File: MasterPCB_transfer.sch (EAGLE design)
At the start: 989 parts, among them IC1 NCS21911SN2T1G, IC10 LDL1117S33R, IC11 LTC4222CUH#PBF, IC12 LTC4222CUH#PBF, IC13 LTC4222CUH#PBF, IC14 LTC4222CUH#PBF, IC15 LTC4222CUH#PBF, IC16 LTC4222CUH#PBF, IC17 LTC4222CUH#PBF, IC18 LTC4222CUH#PBF, IC19 LTC4222CUH#PBF, IC2 NCS21911SN2T1G, IC20 LTC4222CUH#PBF, IC21 LTC4222CUH#PBF, IC22 LTC4222CUH#PBF, IC23 LTC4222CUH#PBF, IC24 NCS21911SN2T1G, IC25 NCS21911SN2T1G, IC26 NCS21911SN2T1G, IC27 NCS21911SN2T1G, IC28 NCS21911SN2T1G, IC29 NCS21911SN2T1G, IC3 NCS21911SN2T1G, IC30 NCS21911SN2T1G, IC31 ADIS16500AMLZ, IC32 LTC6820IUD#PBF, IC33 CBTL01023GM,115, IC34 S35ML04G300WHI000, IC35 S35ML04G300WHI000, IC36 S35ML04G300WHI000, IC37 S35ML04G300WHI000, IC38 ADS8588HIPM, IC39 S35ML04G300WHI000, IC4 LTC4222CUH#PBF, IC40 S35ML04G300WHI000, IC41 S35ML04G300WHI000, IC42 S35ML04G300WHI000, IC43 S35ML04G300WHI000, IC44 S35ML04G300WHI000, IC45 S35ML04G300WHI000, IC46 S35ML04G300WHI000, IC47 S35ML04G300WHI000, IC48 S35ML04G300WHI000, IC49 S35ML04G300WHI000, IC5 LP38692SDX-5.0_NOPB, IC50 S35ML04G300WHI000, IC51 ADS8588HIPM, IC52 ADS8588HIPM, IC55 MUX36S16IRSNR, IC6 LP38692SDX-5.0_NOPB, IC7 LDL1117S33R, IC8 LDL1117S33R, IC9 LP38692SDX-5.0_NOPB, J1 SAMTEC-SMM-104-02-X-DJ, J2 SAMTEC-CLP-106-02-X-DJ, J4 TFM-120-02-L-D, J5 TFM-120-02-L-D, J6 TFM-120-02-L-D, J7 TFM-120-02-L-D, J8 TFM-120-02-L-D, J9 SSM-109-L-SV, M1 NTLUS4C12NTAG, M10 NTLUS4C12NTAG, M11 NTLUS4C12NTAG, M12 NTLUS4C12NTAG, M13 NTLUS4C12NTAG, M14 NTLUS4C12NTAG, M15 NTLUS4C12NTAG, M16 NTLUS4C12NTAG, M17 NTLUS4C12NTAG, M18 NTLUS4C12NTAG, M19 NTLUS4C12NTAG, M2 NTLUS4C12NTAG, M20 NTLUS4C12NTAG, M21 NTLUS4C12NTAG, M22 NTLUS4C12NTAG, M23 NTLUS4C12NTAG, M24 NTLUS4C12NTAG, M25 NTLUS4C12NTAG, M26 NTLUS4C12NTAG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

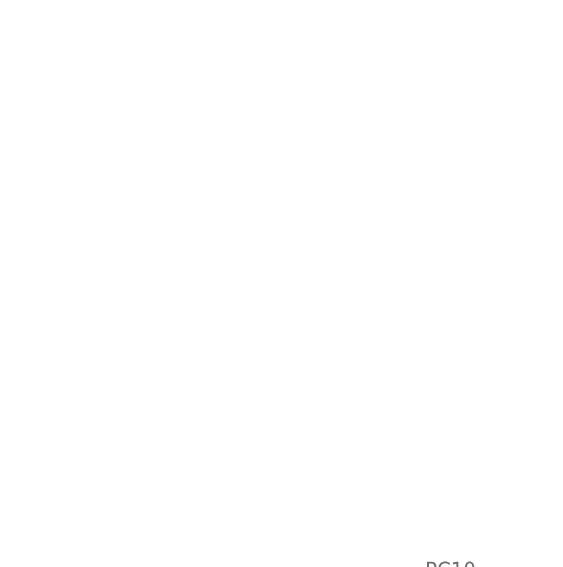
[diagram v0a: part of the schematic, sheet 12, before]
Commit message: Created solid works stripped model of board and setup main board to support layout
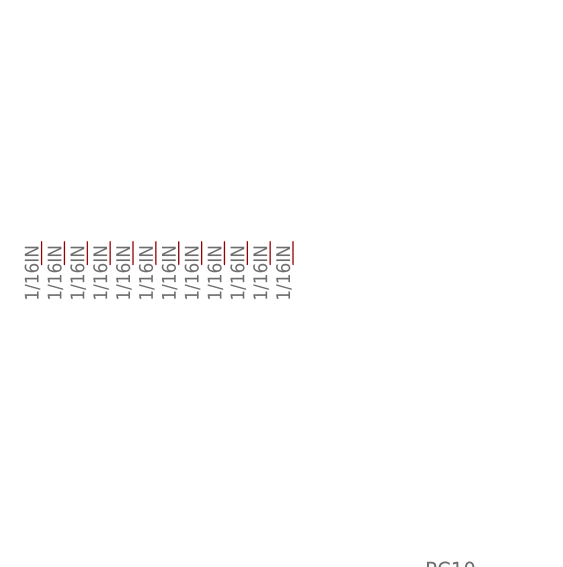
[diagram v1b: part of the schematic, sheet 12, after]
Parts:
- added U$10, U$11, U$12, U$13, U$14, U$15, U$16, U$5, U$6, U$7, U$8, U$9: THROUGH_HOLE, SamacSys_Parts:THROUGH_HOLE
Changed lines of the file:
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@@
 <part name="D87" library="SamacSys_Parts" library_urn="urn:adsk.eagle:library:31941355" deviceset="RSR025N03HZGTL" device="" package3d_urn="urn:adsk.eagle:package:34959477/2"/>
 <part name="J9" library="SamacSys_Parts" library_urn="urn:adsk.eagle:library:31941355" deviceset="SSM-109-L-SV" device="" package3d_urn="urn:adsk.eagle:package:34729422/5"/>
+<part name="U$5" library="SamacSys_Parts" library_urn="urn:adsk.eagle:library:31941355" deviceset="THROUGH_HOLE" device="" package3d_urn="urn:adsk.eagle:package:35094096/3"/>
+<part name="U$6" library="SamacSys_Parts" library_urn="urn:adsk.eagle:library:31941355" deviceset="THROUGH_HOLE" device="" package3d_urn="urn:adsk.eagle:package:35094096/3"/>
+<part name="U$7" library="SamacSys_Parts" library_urn="urn:adsk.eagle:library:31941355" deviceset="THROUGH_HOLE" device="" package3d_urn="urn:adsk.eagle:package:35094096/3"/>
+<part name="U$8" library="SamacSys_Parts" library_urn="urn:adsk.eagle:library:31941355" deviceset="THROUGH_HOLE" device="" package3d_urn="urn:adsk.eagle:package:35094096/3"/>
+<part name="U$9" library="SamacSys_Parts" library_urn="urn:adsk.eagle:library:31941355" deviceset="THROUGH_HOLE" device="" package3d_urn="urn:adsk.eagle:package:35094096/3"/>
+<part name="U$10" library="SamacSys_Parts" library_urn="urn:adsk.eagle:library:31941355" deviceset="THROUGH_HOLE" device="" package3d_urn="urn:adsk.eagle:package:35094096/3"/>
+<part name="U$11" library="SamacSys_Parts" library_urn="urn:adsk.eagle:library:31941355" deviceset="THROUGH_HOLE" device="" package3d_urn="urn:adsk.eagle:package:35094096/3"/>
+<part name="U$12" library="SamacSys_Parts" library_urn="urn:adsk.eagle:library:31941355" deviceset="THROUGH_HOLE" device="" package3d_urn="urn:adsk.eagle:package:35094096/3"/>
+<part name="U$13" library="SamacSys_Parts" library_urn="urn:adsk.eagle:library:31941355" deviceset="THROUGH_HOLE" device="" package3d_urn="urn:adsk.eagle:package:35094096/3"/>
+<part name="U$14" library="SamacSys_Parts" library_urn="urn:adsk.eagle:library:31941355" deviceset="THROUGH_HOLE" device="" package3d_urn="urn:adsk.eagle:package:35094096/3"/>
+<part name="U$15" library="SamacSys_Parts" library_urn="urn:adsk.eagle:library:31941355" deviceset="THROUGH_HOLE" device="" package3d_urn="urn:adsk.eagle:package:35094096/3"/>
+<part name="U$16" library="SamacSys_Parts" library_urn="urn:adsk.eagle:library:31941355" deviceset="THROUGH_HOLE" device="" package3d_urn="urn:adsk.eagle:package:35094096/3"/>
 </parts>
 <sheets>
@@
 <attribute name="VALUE" x="243.84" y="-12.7" size="1.778" layer="96"/>
 </instance>
+<instance part="U$5" gate="G$1" x="-30.48" y="132.08" smashed="yes"/>
+<instance part="U$6" gate="G$1" x="-33.02" y="132.08" smashed="yes"/>
+<instance part="U$7" gate="G$1" x="-35.56" y="132.08" smashed="yes"/>
+<instance part="U$8" gate="G$1" x="-38.1" y="132.08" smashed="yes"/>
+<instance part="U$9" gate="G$1" x="-40.64" y="132.08" smashed="yes"/>
+<instance part="U$10" gate="G$1" x="-43.18" y="132.08" smashed="yes"/>
+<instance part="U$11" gate="G$1" x="-45.72" y="132.08" smashed="yes"/>
+<instance part="U$12" gate="G$1" x="-48.26" y="132.08" smashed="yes"/>
+<instance part="U$13" gate="G$1" x="-50.8" y="132.08" smashed="yes"/>
+<instance part="U$14" gate="G$1" x="-53.34" y="132.08" smashed="yes"/>
+<instance part="U$15" gate="G$1" x="-25.4" y="132.08" smashed="yes"/>
+<instance part="U$16" gate="G$1" x="-27.94" y="132.08" smashed="yes"/>
 </instances>
 <busses>

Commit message: Moving pc, finsihed layout of 7 e-fuses
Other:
- note removed: "2x 16 bit differential single frame capture SAR ADCs that are dedicated for measuring simultaneous outputs from strain gauges. Input signal flow Analog signal -> High input impedance buffer -> Low pass filter BW@~200 hz -> High input impedance buffer -> Digitizing The ADC also applies a 3rd order low pass filter with built in oversampling functionalty. Communication occurs thorugh a serial line."
- note removed: "2x 16 bit differential single frame capture SAR ADCs that are dedicated for measuring simultaneous outputs from strain gauges. Input signal flow Analog signal -> High input impedance buffer -> Low pass filter BW@~200 hz -> High input impedance buffer -> scale input within 5v range -> Digitizing The ADC also applies a 3rd order low pass filter with built in oversampling functionalty. Communication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"
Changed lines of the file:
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@@
 <description>Strain Gauge ADC</description>
 <plain>
-<text x="66.04" y="508" size="1.778" layer="97">2x 16 bit differential single frame capture SAR ADCs that are dedicated for measuring simultaneous outputs from strain gauges.
-Input signal flow
-Analog signal -&gt; High input impedance buffer -&gt; Low pass filter BW@~200 hz -&gt; High input impedance buffer -&gt; Digitizing
-The ADC also applies a 3rd order low pass filter with built in oversampling functionalty.
-Communication occurs thorugh a serial line.</text>
-<rectangle x1="63.5" y1="495.3" x2="213.36" y2="530.86" layer="98"/>
 <text x="210.82" y="228.6" size="1.778" layer="97">From data sheet for split plane conditioning</text>
 <wire x1="208.28" y1="233.68" x2="208.28" y2="226.06" width="0.1524" layer="94"/>
@@
 <description>General and accelerometer ADC</description>
 <plain>
-<text x="30.48" y="233.68" size="1.778" layer="97">2x 16 bit differential single frame capture SAR ADCs that are dedicated for measuring simultaneous outputs from strain gauges.
-Input signal flow
-Analog signal -&gt; High input impedance buffer -&gt; Low pass filter BW@~200 hz -&gt; High input impedance buffer -&gt; scale input within 5v range -&gt; Digitizing
-The ADC also applies a 3rd order low pass filter with built in oversampling functionalty.
-Communication occurs thorugh a serial line.</text>
-<rectangle x1="25.4" y1="226.06" x2="180.34" y2="261.62" layer="98"/>
 <text x="111.76" y="170.18" size="1.778" layer="97">Filter @300hz  with 5/12 reduction</text>
 <wire x1="109.22" y1="175.26" x2="109.22" y2="167.64" width="0.1524" layer="94"/>

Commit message: Check point
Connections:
- removed net ADIN1_8: D33.K
- removed net ADIN1_9: D39.K
- removed net ADIN2_8: D36.K
- net 13.5V_BUS: no longer Z15.1, Z16.1, Z27.1, Z27.4, Z28.1, Z28.4
- net ADIN1_8_POWER_TEMP1: now also D33.K
- net ADIN2_8_POWER_TEMP2: now also D36.K
- net ADIN2_9_POWER_TEMP3: now also D39.K
- net SOURCE1_10: now also Z15.1
- net SOURCE1_11: now also Z25.1
- net SOURCE1_12: now also Z27.1, Z27.4; no longer Z26.4
- net SOURCE2_10: now also Z16.1
- net SOURCE2_11: now also Z26.1, Z26.4; no longer Z25.1
- net SOURCE2_12: now also Z28.1, Z28.4; no longer Z26.1
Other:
- note added: "Single ended digital inputs Splice GND node between 2 sensors 2 sensors share same short circuit protection"
- note removed: "Single ended digital inputs Splice GND node between 2 sensors"
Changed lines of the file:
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@@
 <wire x1="495.3" y1="967.74" x2="495.3" y2="911.86" width="0.1524" layer="94"/>
 <wire x1="495.3" y1="911.86" x2="10.16" y2="911.86" width="0.1524" layer="94"/>
-<text x="-38.1" y="937.26" size="1.778" layer="97">Single ended digital inputs
-Splice GND node between 2 sensors</text>
-<wire x1="-40.64" y1="944.88" x2="-40.64" y2="934.72" width="0.1524" layer="94"/>
-<wire x1="-40.64" y1="934.72" x2="5.08" y2="934.72" width="0.1524" layer="94"/>
+<text x="-45.72" y="937.26" size="1.778" layer="97">Single ended digital inputs
+Splice GND node between 2 sensors
+2 sensors share same short circuit protection</text>
+<wire x1="-48.26" y1="944.88" x2="-48.26" y2="934.72" width="0.1524" layer="94"/>
+<wire x1="-48.26" y1="934.72" x2="5.08" y2="934.72" width="0.1524" layer="94"/>
 <wire x1="5.08" y1="934.72" x2="5.08" y2="944.88" width="0.1524" layer="94"/>
-<wire x1="5.08" y1="944.88" x2="-40.64" y2="944.88" width="0.1524" layer="94"/>
+<wire x1="5.08" y1="944.88" x2="-48.26" y2="944.88" width="0.1524" layer="94"/>
 <text x="-43.18" y="76.2" size="1.778" layer="97">Visual indicator that power is available
 to the node at this segment of the board</text>
@@
 </segment>
 <segment>
-<pinref part="Z27" gate="Z$1" pin="1"/>
-<wire x1="347.98" y1="947.42" x2="353.06" y2="947.42" width="0.1524" layer="91"/>
-<label x="350.52" y="949.96" size="1.778" layer="95"/>
-</segment>
-<segment>
-<pinref part="Z28" gate="Z$1" pin="1"/>
-<wire x1="477.52" y1="947.42" x2="482.6" y2="947.42" width="0.1524" layer="91"/>
-<label x="480.06" y="949.96" size="1.778" layer="95"/>
-</segment>
-<segment>
 <pinref part="R424" gate="G$1" pin="2"/>
 <wire x1="312.42" y1="876.3" x2="309.88" y2="876.3" width="0.1524" layer="91"/>
@@
 </segment>
 <segment>
-<pinref part="Z27" gate="Z$1" pin="4"/>
-<wire x1="322.58" y1="947.42" x2="317.5" y2="947.42" width="0.1524" layer="91"/>
-<label x="312.42" y="949.96" size="1.778" layer="95"/>
-</segment>
-<segment>
-<pinref part="Z28" gate="Z$1" pin="4"/>
-<wire x1="452.12" y1="947.42" x2="447.04" y2="947.42" width="0.1524" layer="91"/>
-<label x="441.96" y="949.96" size="1.778" layer="95"/>
-</segment>
-<segment>
 <pinref part="R445" gate="G$1" pin="1"/>
 <wire x1="17.78" y1="96.52" x2="17.78" y2="99.06" width="0.1524" layer="91"/>
@@
 <label x="276.86" y="843.28" size="1.778" layer="95"/>
 </segment>
-<segment>
-<pinref part="Z15" gate="Z$1" pin="1"/>
-<wire x1="871.22" y1="701.04" x2="876.3" y2="701.04" width="0.1524" layer="91"/>
-<label x="876.3" y="698.5" size="1.778" layer="95"/>
-</segment>
-<segment>
-<pinref part="Z16" gate="Z$1" pin="1"/>
-<wire x1="1000.76" y1="701.04" x2="1005.84" y2="701.04" width="0.1524" layer="91"/>
-<label x="1005.84" y="698.5" size="1.778" layer="95"/>
-</segment>
 </net>
 <net name="N$33" class="0">
@@
 </segment>
 </net>
-<net name="ADIN1_8" class="0">
-<segment>
-<pinref part="D33" gate="G$1" pin="K"/>
-<wire x1="365.76" y1="695.96" x2="365.76" y2="698.5" width="0.1524" layer="91"/>
-<label x="368.3" y="698.5" size="1.778" layer="95" rot="R90"/>
-</segment>
-</net>
-<net name="ADIN2_8" class="0">
-<segment>
-<pinref part="D36" gate="G$1" pin="K"/>
-<wire x1="495.3" y1="695.96" x2="495.3" y2="698.5" width="0.1524" layer="91"/>
-<label x="497.84" y="698.5" size="1.778" layer="95" rot="R90"/>
-</segment>
-</net>
 <net name="GPIO2_8" class="0">
 <segment>
@@
 </segment>
 </net>
-<net name="ADIN1_9" class="0">
-<segment>
-<pinref part="D39" gate="G$1" pin="K"/>
-<wire x1="624.84" y1="695.96" x2="624.84" y2="698.5" width="0.1524" layer="91"/>
-<label x="627.38" y="698.5" size="1.778" layer="95" rot="R90"/>
-</segment>
-</net>
 <net name="ADIN2_9_POWER_TEMP3" class="0">
 <segment>
@@
 <label x="591.82" y="675.64" size="1.778" layer="95"/>
 </segment>
+<segment>
+<pinref part="D39" gate="G$1" pin="K"/>
+<wire x1="624.84" y1="695.96" x2="624.84" y2="698.5" width="0.1524" layer="91"/>
+<label x="627.38" y="698.5" size="1.778" layer="95" rot="R90"/>
+</segment>
 </net>
 <net name="GPIO2_9" class="0">
@@
 <label x="1003.3" y="624.84" size="1.778" layer="95"/>
 </segment>
+<segment>
+<pinref part="Z15" gate="Z$1" pin="1"/>
+<wire x1="871.22" y1="701.04" x2="876.3" y2="701.04" width="0.1524" layer="91"/>
+<label x="876.3" y="698.5" size="1.778" layer="95"/>
+</segment>
 </net>
 <net name="FB1_10" class="0">
@@
 <label x="924.56" y="497.84" size="1.778" layer="95" rot="MR180"/>
 </segment>
+<segment>
+<pinref part="Z16" gate="Z$1" pin="1"/>
+<wire x1="1000.76" y1="701.04" x2="1005.84" y2="701.04" width="0.1524" layer="91"/>
+<label x="1005.84" y="698.5" size="1.778" layer="95"/>
+</segment>
 </net>
 <net name="GATE2_10" class="0">
@@
 </segment>
 <segment>
-<pinref part="Z25" gate="Z$1" pin="1"/>
-<wire x1="83.82" y1="944.88" x2="88.9" y2="944.88" width="0.1524" layer="91"/>
-<label x="86.36" y="947.42" size="1.778" layer="95"/>
+<pinref part="Z26" gate="Z$1" pin="4"/>
+<wire x1="187.96" y1="944.88" x2="182.88" y2="944.88" width="0.1524" layer="91"/>
+<label x="177.8" y="947.42" size="1.778" layer="95"/>
+</segment>
+<segment>
+<pinref part="Z26" gate="Z$1" pin="1"/>
+<wire x1="213.36" y1="944.88" x2="218.44" y2="944.88" width="0.1524" layer="91"/>
+<label x="215.9" y="947.42" size="1.778" layer="95"/>
 </segment>
 </net>
@@
 <label x="48.26" y="947.42" size="1.778" layer="95"/>
 </segment>
+<segment>
+<pinref part="Z25" gate="Z$1" pin="1"/>
+<wire x1="83.82" y1="944.88" x2="88.9" y2="944.88" width="0.1524" layer="91"/>
+<label x="86.36" y="947.42" size="1.778" layer="95"/>
+</segment>
 </net>
 <net name="GATE2_11" class="0">
@@
 </segment>
 <segment>
-<pinref part="Z26" gate="Z$1" pin="4"/>
-<wire x1="187.96" y1="944.88" x2="182.88" y2="944.88" width="0.1524" layer="91"/>
-<label x="177.8" y="947.42" size="1.778" layer="95"/>
+<pinref part="Z27" gate="Z$1" pin="4"/>
+<wire x1="322.58" y1="947.42" x2="317.5" y2="947.42" width="0.1524" layer="91"/>
+<label x="312.42" y="949.96" size="1.778" layer="95"/>
+</segment>
+<segment>
+<pinref part="Z27" gate="Z$1" pin="1"/>
+<wire x1="347.98" y1="947.42" x2="353.06" y2="947.42" width="0.1524" layer="91"/>
+<label x="350.52" y="949.96" size="1.778" layer="95"/>
 </segment>
 </net>
@@
 </segment>
 <segment>
-<pinref part="Z26" gate="Z$1" pin="1"/>
-<wire x1="213.36" y1="944.88" x2="218.44" y2="944.88" width="0.1524" layer="91"/>
-<label x="215.9" y="947.42" size="1.778" layer="95"/>
+<pinref part="Z28" gate="Z$1" pin="4"/>
+<wire x1="452.12" y1="947.42" x2="447.04" y2="947.42" width="0.1524" layer="91"/>
+<label x="441.96" y="949.96" size="1.778" layer="95"/>
+</segment>
+<segment>
+<pinref part="Z28" gate="Z$1" pin="1"/>
+<wire x1="477.52" y1="947.42" x2="482.6" y2="947.42" width="0.1524" layer="91"/>
+<label x="480.06" y="949.96" size="1.778" layer="95"/>
 </segment>
 </net>
@@
 <label x="332.74" y="675.64" size="1.778" layer="95"/>
 </segment>
+<segment>
+<pinref part="D33" gate="G$1" pin="K"/>
+<wire x1="365.76" y1="695.96" x2="365.76" y2="698.5" width="0.1524" layer="91"/>
+<label x="368.3" y="698.5" size="1.778" layer="95" rot="R90"/>
+</segment>
 </net>
 <net name="ADIN2_8_POWER_TEMP2" class="0">
@@
 <label x="462.28" y="675.64" size="1.778" layer="95"/>
 </segment>
+<segment>
+<pinref part="D36" gate="G$1" pin="K"/>
+<wire x1="495.3" y1="695.96" x2="495.3" y2="698.5" width="0.1524" layer="91"/>
+<label x="497.84" y="698.5" size="1.778" layer="95" rot="R90"/>
+</segment>
 </net>

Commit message: Dangerous maneuvers currently... Board reshaping
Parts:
- removed U$11, U$16: THROUGH_HOLE, SamacSys_Parts:THROUGH_HOLE
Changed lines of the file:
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@@
 <part name="U$9" library="SamacSys_Parts" library_urn="urn:adsk.eagle:library:31941355" deviceset="THROUGH_HOLE" device="" package3d_urn="urn:adsk.eagle:package:35094096/3"/>
 <part name="U$10" library="SamacSys_Parts" library_urn="urn:adsk.eagle:library:31941355" deviceset="THROUGH_HOLE" device="" package3d_urn="urn:adsk.eagle:package:35094096/3"/>
-<part name="U$11" library="SamacSys_Parts" library_urn="urn:adsk.eagle:library:31941355" deviceset="THROUGH_HOLE" device="" package3d_urn="urn:adsk.eagle:package:35094096/3"/>
 <part name="U$12" library="SamacSys_Parts" library_urn="urn:adsk.eagle:library:31941355" deviceset="THROUGH_HOLE" device="" package3d_urn="urn:adsk.eagle:package:35094096/3"/>
 <part name="U$13" library="SamacSys_Parts" library_urn="urn:adsk.eagle:library:31941355" deviceset="THROUGH_HOLE" device="" package3d_urn="urn:adsk.eagle:package:35094096/3"/>
 <part name="U$14" library="SamacSys_Parts" library_urn="urn:adsk.eagle:library:31941355" deviceset="THROUGH_HOLE" device="" package3d_urn="urn:adsk.eagle:package:35094096/3"/>
 <part name="U$15" library="SamacSys_Parts" library_urn="urn:adsk.eagle:library:31941355" deviceset="THROUGH_HOLE" device="" package3d_urn="urn:adsk.eagle:package:35094096/3"/>
-<part name="U$16" library="SamacSys_Parts" library_urn="urn:adsk.eagle:library:31941355" deviceset="THROUGH_HOLE" device="" package3d_urn="urn:adsk.eagle:package:35094096/3"/>
 </parts>
 <sheets>
@@
 <instance part="U$9" gate="G$1" x="-40.64" y="132.08" smashed="yes"/>
 <instance part="U$10" gate="G$1" x="-43.18" y="132.08" smashed="yes"/>
-<instance part="U$11" gate="G$1" x="-45.72" y="132.08" smashed="yes"/>
 <instance part="U$12" gate="G$1" x="-48.26" y="132.08" smashed="yes"/>
 <instance part="U$13" gate="G$1" x="-50.8" y="132.08" smashed="yes"/>
 <instance part="U$14" gate="G$1" x="-53.34" y="132.08" smashed="yes"/>
 <instance part="U$15" gate="G$1" x="-25.4" y="132.08" smashed="yes"/>
-<instance part="U$16" gate="G$1" x="-27.94" y="132.08" smashed="yes"/>
 </instances>
 <busses>

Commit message: swapping
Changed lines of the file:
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@@
 </instance>
 <instance part="C13" gate="G$1" x="220.98" y="393.7" smashed="yes" rot="R90">
-<attribute name="NAME" x="214.63" y="402.59" size="1.778" layer="95" rot="R90" align="center-left"/>
+<attribute name="NAME" x="222.25" y="389.89" size="1.778" layer="95" rot="R90" align="center-left"/>
 <attribute name="VALUE" x="217.17" y="402.59" size="1.778" layer="96" rot="R90" align="center-left"/>
 </instance>
 <instance part="C1" gate="G$1" x="228.6" y="393.7" smashed="yes" rot="R90">
-<attribute name="NAME" x="222.25" y="402.59" size="1.778" layer="95" rot="R90" align="center-left"/>
+<attribute name="NAME" x="227.33" y="389.89" size="1.778" layer="95" rot="R90" align="center-left"/>
 <attribute name="VALUE" x="224.79" y="402.59" size="1.778" layer="96" rot="R90" align="center-left"/>
 </instance>

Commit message: layout has been placed
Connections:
- net IM_OUT1: now also R516.1
- net IM_OUTPUT: no longer R516.1
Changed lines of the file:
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@@
 <label x="33.02" y="114.3" size="1.778" layer="95" rot="R180"/>
-</segment>
-<segment>
-<pinref part="R516" gate="G$1" pin="1"/>
-<wire x1="53.34" y1="111.76" x2="55.88" y2="111.76" width="0.1524" layer="91"/>
-<label x="55.88" y="111.76" size="1.778" layer="95"/>
 </segment>
 </net>
@@
 <label x="127" y="91.44" size="1.778" layer="95"/>
 </segment>
+<segment>
+<pinref part="R516" gate="G$1" pin="1"/>
+<wire x1="53.34" y1="111.76" x2="55.88" y2="111.76" width="0.1524" layer="91"/>
+<label x="55.88" y="111.76" size="1.778" layer="95"/>
+</segment>
 </net>

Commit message: Moving PC
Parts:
- IC37: SPICEPREFIX (none) -> X

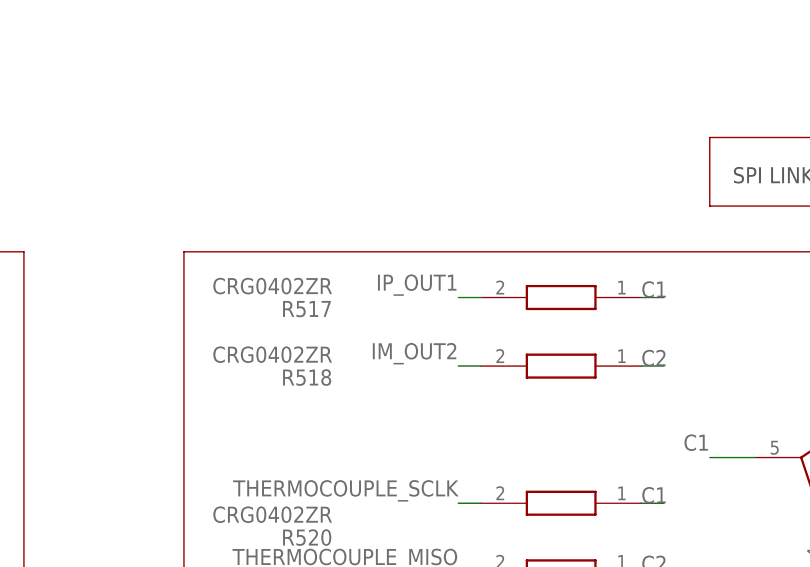
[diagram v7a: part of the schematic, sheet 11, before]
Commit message: Minor changes, should only been a change of board stack up
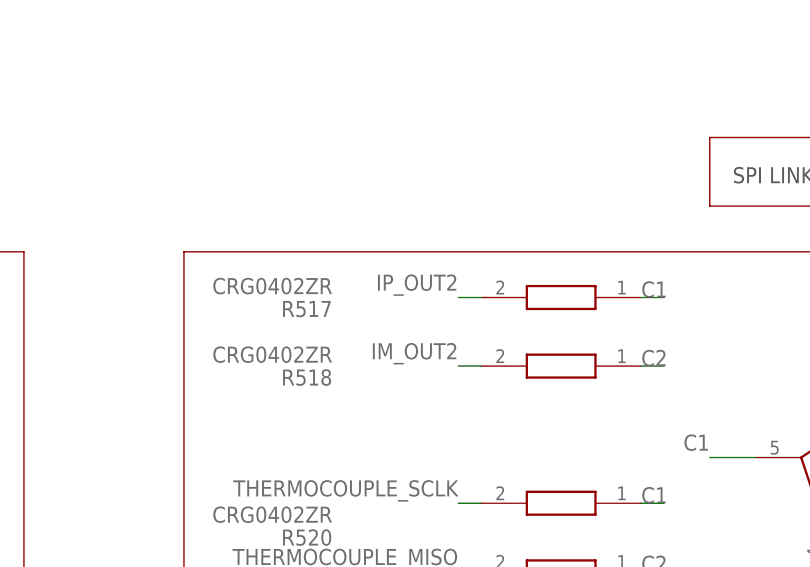
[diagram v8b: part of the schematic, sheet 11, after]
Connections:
- net IP_OUT1: no longer R517.2
- net IP_OUT2: now also R517.2
